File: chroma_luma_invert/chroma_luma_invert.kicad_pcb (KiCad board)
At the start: 2 copper layers, 100 x 100 mm, 59 parts, among them J1 rca, J2 rca, J3 Barrel_Jack, J4 Conn_01x12, SW1 SW_SPST, SW2 SW_SPST, U1 AD8042, U10 74HC4538, U2 AD8042, U3 4051, U4 LM317, U5 LM311, U6 LM311, U7 74HC4538, U8 74HC4538, U9 4040

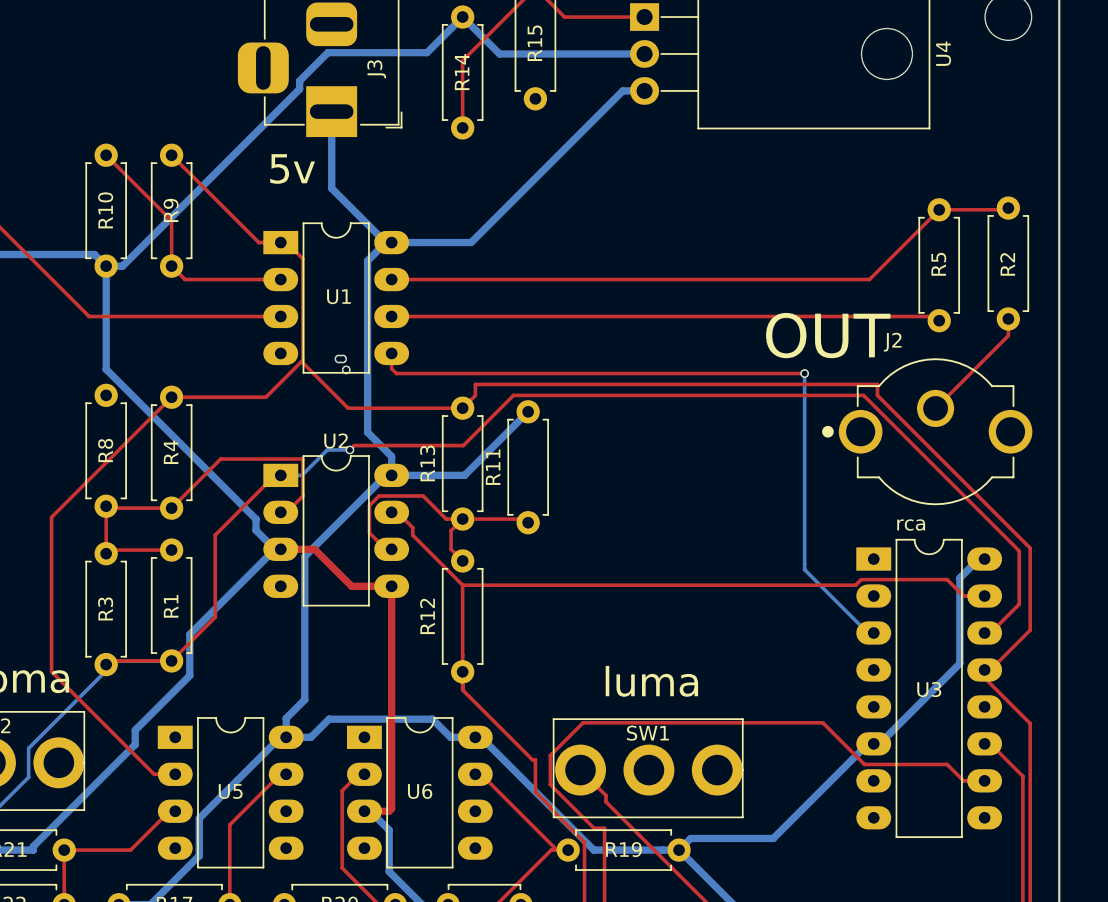
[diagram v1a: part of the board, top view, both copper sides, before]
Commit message: updated opamp
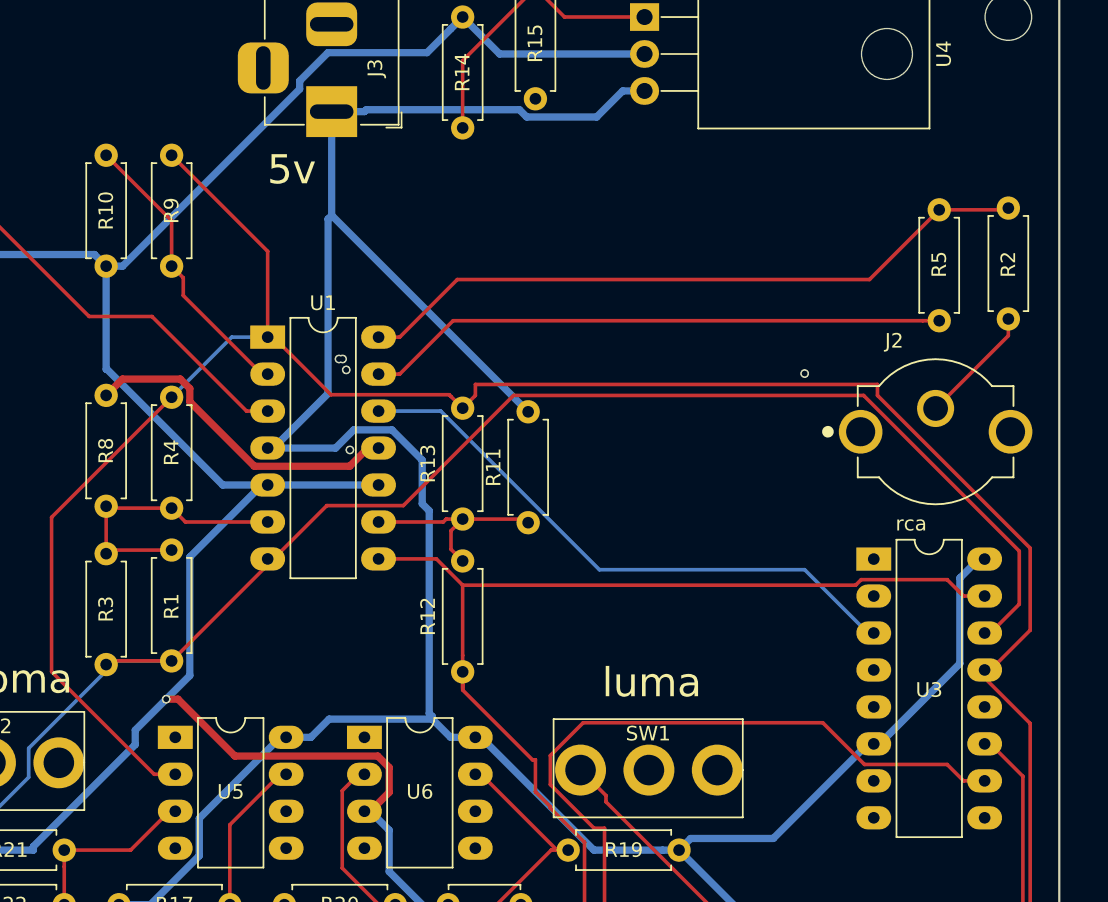
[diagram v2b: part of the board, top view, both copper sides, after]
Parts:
- removed U2: AD8042, Package_DIP:DIP-8_W7.62mm_LongPads
- U1: value AD8042 -> AD8044; footprint Package_DIP:DIP-8_W7.62mm_LongPads -> Package_DIP:DIP-14_W7.62mm_LongPads
- moved U1 6.56 mm to (150.6, 60.5)
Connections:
- U1 pad 4: GND -> +5V
- U1 pad 5: Net-(U1-Pad5) -> 2.5V
- U1 pad 6: Net-(R5-Pad2) -> Net-(R1-Pad2)
- U1 pad 7: Net-(R2-Pad2) -> invert_video
- U1 pad 8: +5V -> invert_burst
- U3 pad 3: Net-(U1-Pad5) -> Net-(U1-Pad12)
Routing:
- net Net-(U1-Pad5): track 49.6 -> 0.00 mm, vias 1 -> 0
- net Net-(U1-Pad12): track 0.00 -> 40.3 mm, vias 0 -> 1
- net GND: track 0.00 -> 22.7 mm
- net +5V: track 365.5 -> 380.1 mm
- net Net-(R1-Pad2): track 27.3 -> 19.4 mm
- net Net-(R11-Pad1): track 19.4 -> 14.0 mm
- net 2.5V: track 196.4 -> 200.6 mm, vias 0 -> 1
- net invert_video: track 174.7 -> 171.2 mm
- net Net-(R5-Pad2): track 37.8 -> 40.5 mm
- net Net-(R2-Pad2): track 44.4 -> 47.0 mm
- net Net-(R10-Pad1): track 17.4 -> 19.9 mm
- net original_video: track 216.5 -> 214.1 mm
- net Net-(C1-Pad1): track 51.3 -> 53.1 mm
- net invert_burst: track 116.4 -> 115.7 mm
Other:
- board text removed: "OUT"

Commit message: updated two_comparator and added two_point_one
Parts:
- removed REF** (x4): MountingHole_3.2mm_M3, Mounting_Holes:MountingHole_3.2mm_M3
- removed the U5 at (144.2, 88.0)
- removed the U6 at (157.2, 88.0)
- added C10: 0.1u, Capacitor_THT:C_Disc_D4.7mm_W2.5mm_P5.00mm, F.Cu at (209.1, 85.3)
- added C11: 0.1u, Capacitor_THT:C_Disc_D4.7mm_W2.5mm_P5.00mm, F.Cu at (217.2, 81.2)
- added C12: 0.1u, Capacitor_THT:C_Disc_D4.7mm_W2.5mm_P5.00mm, F.Cu at (209.1, 89.3)
- added C13: 0.1u, Capacitor_THT:C_Disc_D4.7mm_W2.5mm_P5.00mm, F.Cu at (217.2, 85.3)
- added C14: 0.1u, Capacitor_THT:C_Disc_D4.7mm_W2.5mm_P5.00mm, F.Cu at (225.4, 81.2)
- added C15: 0.1u, Capacitor_THT:C_Disc_D4.7mm_W2.5mm_P5.00mm, F.Cu at (217.2, 89.3)
- added C8: 10uf, Capacitor_THT:CP_Radial_D6.3mm_P2.50mm, F.Cu at (226.6, 87.2)
- added C9: 0.1u, Capacitor_THT:C_Disc_D4.7mm_W2.5mm_P5.00mm, F.Cu at (209.1, 81.2)
- added U2: LM393, Package_DIP:DIP-8_W7.62mm_LongPads, F.Cu at (237.6, 81.3)
- R21: value 10k -> 3.9k
- R22: value 3.9k -> 10k
- R8: value 2.2 -> 2.2k
- renumbered U10 to U5, U9 to U6
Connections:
- R16 pad 1: Net-(C2-Pad1) -> Net-(C2-Pad2)
- R18 pad 1: Net-(C3-Pad1) -> Net-(C3-Pad2)
- R24 pad 1: Net-(C5-Pad1) -> Net-(C5-Pad2)
- R25 pad 1: Net-(C6-Pad1) -> Net-(C6-Pad2)
- R26 pad 1: Net-(C7-Pad1) -> Net-(C7-Pad2)
- U3 pad 6: +5V -> GND
- U6 pad 10: v_sync -> sync
- U6 pad 11: sync -> v_sync
- U6 pad 12: Net-(U8-Pad5) -> Net-(U6-Pad12)
- U8 pad 4: GND -> Net-(U6-Pad12)
- U8 pad 5: Net-(U8-Pad5) -> +5V
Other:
- board text added: "OUT"
- board text added: "chroma_luma_invert v0.2 by Rob Schafer pcb by cyberboy666"
- board text removed: "chroma_luma_invert v0.1 by Rob Schafer pcb by cyberboy666"

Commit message: revised all boards
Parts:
- added C16: 0.001u, Capacitor_THT:C_Disc_D4.7mm_W2.5mm_P5.00mm, F.Cu at (133.7, 72.7)
- added REF**: MountingHole_3.2mm_M3, MountingHole:MountingHole_3.2mm_M3, F.Cu at (201.5, 38.6)
- added REF**: MountingHole_3.2mm_M3, MountingHole:MountingHole_3.2mm_M3, F.Cu at (201.6, 131.4)
- added REF**: MountingHole_3.2mm_M3, MountingHole:MountingHole_3.2mm_M3, F.Cu at (108.4, 131.3)
- added REF**: MountingHole_3.2mm_M3, MountingHole:MountingHole_3.2mm_M3, F.Cu at (108.5, 38.6)
- added RV5: 1k_trim, lib_fp:tht_vertical_trimpot_3362, F.Cu at (176.3, 82.5)
- added RV6: 1k_trim, lib_fp:tht_vertical_trimpot_3362, F.Cu at (130.9, 82.3)
- added RV7: 1k_trim, lib_fp:tht_vertical_trimpot_3362, F.Cu at (130.9, 75.2)
- J1, J2: footprint lib_fp:RCJ-024 -> lib_fp:tht_vertical_rca
- R3: value 1k -> 1.5k
- RV1: value 10k_pot -> 10k_trim; footprint lib_fp:Pot_trim_3362_tayda -> lib_fp:tht_vertical_trimpot_3362
- RV2: value 5k_pot -> 5k_trim; footprint lib_fp:Pot_trim_3362_tayda -> lib_fp:tht_vertical_trimpot_3362
- RV3: value 100k_pot -> 100k_trim; footprint lib_fp:Pot_trim_3362_tayda -> lib_fp:tht_vertical_trimpot_3362
- RV4: value 20k_pot -> 20k_trim; footprint lib_fp:Pot_trim_3362_tayda -> lib_fp:tht_vertical_trimpot_3362
- SW1, SW2: value SW_SPST -> SPDT
- U1: footprint Package_DIP:DIP-14_W7.62mm_LongPads -> project_parts:DIP+SOIC_14
- U3: value 4051 -> CD4051
- U6: value 4040 -> CD4040
- moved C8 95.8 mm to (143.0, 40.4)
- moved C11 95.4 mm to (124.1, 102.1), turned to 270 degrees
- moved C9 91.1 mm to (118.0, 78.0)
- moved U2 87.1 mm to (151.5, 94.2), turned to 90 degrees
- moved C13 69.4 mm to (148.1, 91.3), turned to 90 degrees
- moved C10 69.2 mm to (144.7, 110.6), turned to 90 degrees
- moved C15 61.8 mm to (155.9, 81.6), turned to 180 degrees
- moved C14 31.1 mm to (194.9, 74.9)
- moved C12 20.6 mm to (190.6, 98.5), turned to 270 degrees
- moved U1 3.01 mm to (153.5, 61.3)
- moved R18 2.27 mm to (179.8, 101.7)
- moved U3 2.15 mm to (192.2, 77.9)
- moved R26 1.53 mm to (113.5, 106.3)
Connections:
- R3 pad 2: Net-(R1-Pad2) -> Net-(R3-Pad2)
- R4 pad 1: Net-(R1-Pad2) -> Net-(R3-Pad2)
- R8 pad 2: Net-(R1-Pad2) -> Net-(R3-Pad2)
- U1 pad 6: Net-(R1-Pad2) -> Net-(R3-Pad2)
- U3 pad 15: invert_burst -> Net-(C16-Pad1)
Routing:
- net Net-(C16-Pad1): track 0.00 -> 122.9 mm
- net Net-(R11-Pad1): track 14.0 -> 115.7 mm, vias 0 -> 1
- net Net-(R3-Pad2): track 0.00 -> 86.7 mm
- net +5V: track 380.1 -> 466.5 mm
- net invert_burst: track 115.7 -> 188.2 mm, vias 0 -> 1
- net Net-(U6-Pad12): track 0.00 -> 51.0 mm
- net Net-(U8-Pad5): track 50.6 -> 0.00 mm
- net 2.5V: track 200.6 -> 234.1 mm, vias 1 -> 0
- net Net-(C1-Pad1): track 53.1 -> 86.6 mm
- net Net-(R10-Pad1): track 19.9 -> 50.5 mm
- net invert_video: track 171.2 -> 200.3 mm, vias 3 -> 2
- net v_sync: track 59.9 -> 82.0 mm, vias 0 -> 1
- net original_video: track 214.1 -> 234.1 mm
- net Net-(R1-Pad2): track 19.4 -> 0.00 mm
- net GND: track 22.7 -> 41.9 mm
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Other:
- board text added: "<-"
- board text added: "_^ XX"
- board text added: "chroma_luma_invert v0_2 based on Rob Schafer design updated by cyberboy666"
- board text added: "underscores.shop"
- board text removed: "chroma_luma_invert v0.2 by Rob Schafer pcb by cyberboy666"
